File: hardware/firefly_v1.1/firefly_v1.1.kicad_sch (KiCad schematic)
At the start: 8 parts, among them J1 Button cell battery, Q1 IRLML6344, U1 MSP430G2231IN14

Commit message: Initial placement done
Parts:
- added J2: Conn_01x04, Connector_PinHeader_2.54mm:PinHeader_1x04_P2.54mm_Vertical, symbol Connector_Generic:Conn_01x04
- C1: footprint (none) -> Capacitor_SMD:C_1210_3225Metric_Pad1.33x2.70mm_HandSolder
- D1: footprint (none) -> LED_SMD:LED_0805_2012Metric_Pad1.15x1.40mm_HandSolder
- D2: footprint (none) -> TestPoint:TestPoint_2Pads_Pitch2.54mm_Drill0.8mm
- J1: value Button cell battery -> Conn_01x02; footprint (none) -> Capacitor_SMD:C_1210_3225Metric_Pad1.33x2.70mm_HandSolder
- L1: footprint (none) -> LIB_HM79M-20102LFTR:HM79M20102LFTR
- R1: footprint (none) -> Resistor_SMD:R_0603_1608Metric_Pad0.98x0.95mm_HandSolder
- U1: footprint Package_SO:TSSOP-14_4.4x5mm_P0.65mm -> Package_DIP:DIP-14_W7.62mm
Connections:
- net GND: now also J2.2 (Pin_2)
- net at C1.1, D2.1 (K), J1.2 (Pin_2)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: now also J2.1 (Pin_1)
- net at R1.2, U1.10 (~{RST}/NMI/SBWTDIO): now also J2.4 (Pin_4)
- net at U1.11 (SBWTCK/TEST): now also J2.3 (Pin_3)
- no-connect marks 8 -> 7

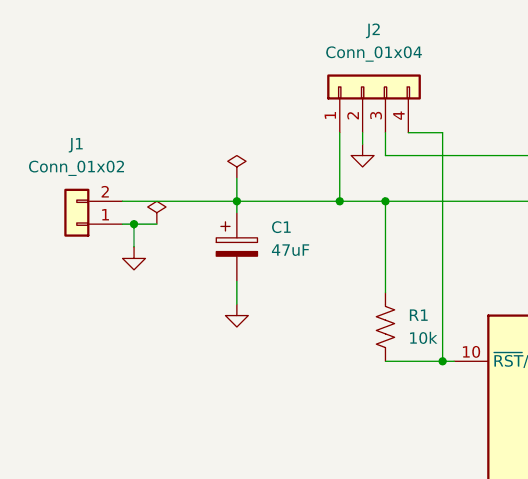
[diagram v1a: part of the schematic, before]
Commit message: Completed routing
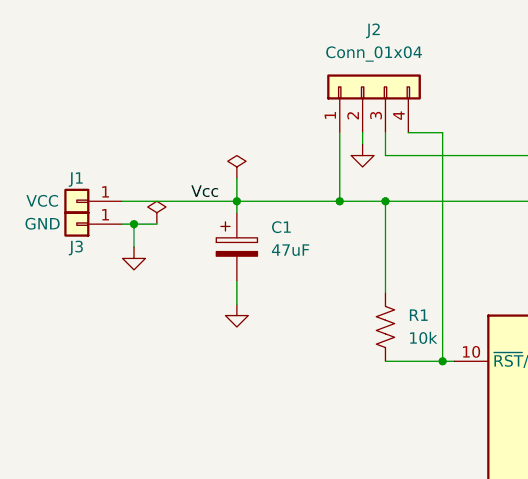
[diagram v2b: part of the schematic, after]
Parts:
- removed J1: Conn_01x02, Capacitor_SMD:C_1210_3225Metric_Pad1.33x2.70mm_HandSolder, symbol Connector_Generic:Conn_01x02
- added J1: VCC, TestPoint:TestPoint_Pad_D1.5mm, symbol Connector_Generic:Conn_01x01
- added J3: GND, TestPoint:TestPoint_Pad_D1.5mm, symbol Connector_Generic:Conn_01x01
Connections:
- net GND: now also J3.1 (Pin_1)
- net Vcc: now reaches C1.1, D2.1 (K), J2.1 (Pin_1), L1.1, R1.1, U1.1 (DVCC)
- net Vcc: now also J1.1 (Pin_1)
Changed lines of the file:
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@@
     (stroke (width 0) (type default))
   )
+  (label "Vcc" (at 80.01 69.85 0) (fields_autoplaced)
+    (effects (font (size 1.27 1.27)) (justify left bottom))
+  )
   (symbol (lib_id "power:GND") (at 73.66 74.93 0) (unit 1)
     (in_bom yes) (on_board yes) (dnp no) (fields_autoplaced)
@@
         (path "/c3df62b2-e3a5-4c68-9c14-2172467d02fe"
           (reference "#PWR01") (unit 1)
+        )
+      )
+    )
+  )
+  (symbol (lib_id "Connector_Generic:Conn_01x01") (at 67.31 72.39 180) (unit 1)
+    (in_bom yes) (on_board yes) (dnp no)
+    (property "Reference" "J3" (at 67.31 74.93 0)
+      (effects (font (size 1.27 1.27)))
+    )
+    (property "Value" "GND" (at 63.5 72.39 0)
+      (effects (font (size 1.27 1.27)))
+    )
+    (property "Footprint" "TestPoint:TestPoint_Pad_D1.5mm" (at 67.31 72.39 0)
+      (effects (font (size 1.27 1.27)) hide)
+    )
+    (property "Datasheet" "~" (at 67.31 72.39 0)
+      (effects (font (size 1.27 1.27)) hide)
+    )
+    (pin "1")
+    (instances
+      (project "firefly_v1.1"
+        (path "/c3df62b2-e3a5-4c68-9c14-2172467d02fe"
+          (reference "J3") (unit 1)
         )
       )
@@
         (path "/c3df62b2-e3a5-4c68-9c14-2172467d02fe"
           (reference "D1") (unit 1)
+        )
+      )
+    )
+  )
+  (symbol (lib_id "Connector_Generic:Conn_01x01") (at 67.31 69.85 180) (unit 1)
+    (in_bom yes) (on_board yes) (dnp no)
+    (property "Reference" "J1" (at 67.31 67.31 0)
+      (effects (font (size 1.27 1.27)))
+    )
+    (property "Value" "VCC" (at 63.5 69.85 0)
+      (effects (font (size 1.27 1.27)))
+    )
+    (property "Footprint" "TestPoint:TestPoint_Pad_D1.5mm" (at 67.31 69.85 0)
+      (effects (font (size 1.27 1.27)) hide)
+    )
+    (property "Datasheet" "~" (at 67.31 69.85 0)
+      (effects (font (size 1.27 1.27)) hide)
+    )
+    (pin "1")
+    (instances
+      (project "firefly_v1.1"
+        (path "/c3df62b2-e3a5-4c68-9c14-2172467d02fe"
+          (reference "J1") (unit 1)
         )
       )
@@
         )
       )
-    )
-  )
-  (symbol (lib_id "Connector_Generic:Conn_01x02") (at 67.31 72.39 180) (unit 1)
-    (in_bom yes) (on_board yes) (dnp no) (fields_autoplaced)
-    (property "Reference" "J1" (at 67.31 63.5 0)
-      (effects (font (size 1.27 1.27)))
-    )
-    (property "Value" "Conn_01x02" (at 67.31 66.04 0)
-      (effects (font (size 1.27 1.27)))
-    )
-    (property "Footprint" "Capacitor_SMD:C_1210_3225Metric_Pad1.33x2.70mm_HandSolder" (at 67.31 72.39 0)
-      (effects (font (size 1.27 1.27)) hide)
-    )
-    (property "Datasheet" "~" (at 67.31 72.39 0)
-      (effects (font (size 1.27 1.27)) hide)
-    )
-    (pin "1")
-    (pin "2")
-    (instances
-      (project "firefly_v1.1"
-        (path "/c3df62b2-e3a5-4c68-9c14-2172467d02fe"
-          (reference "J1") (unit 1)
-        )
-      )
